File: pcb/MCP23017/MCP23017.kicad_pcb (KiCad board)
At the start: 2 copper layers, 15 parts, among them U1 MCP23017, U2 Header2

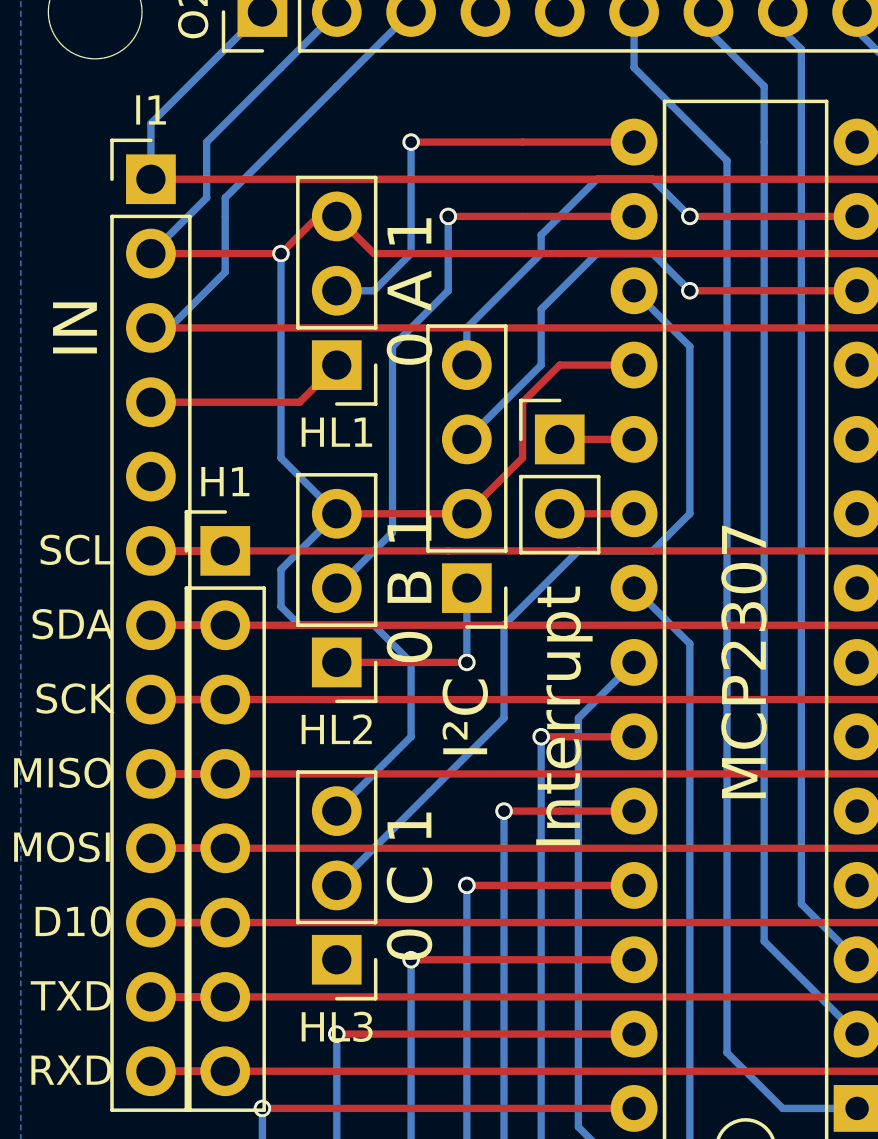
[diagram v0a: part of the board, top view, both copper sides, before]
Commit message: Added a new "power" and LEDs module (split into two half size modules)
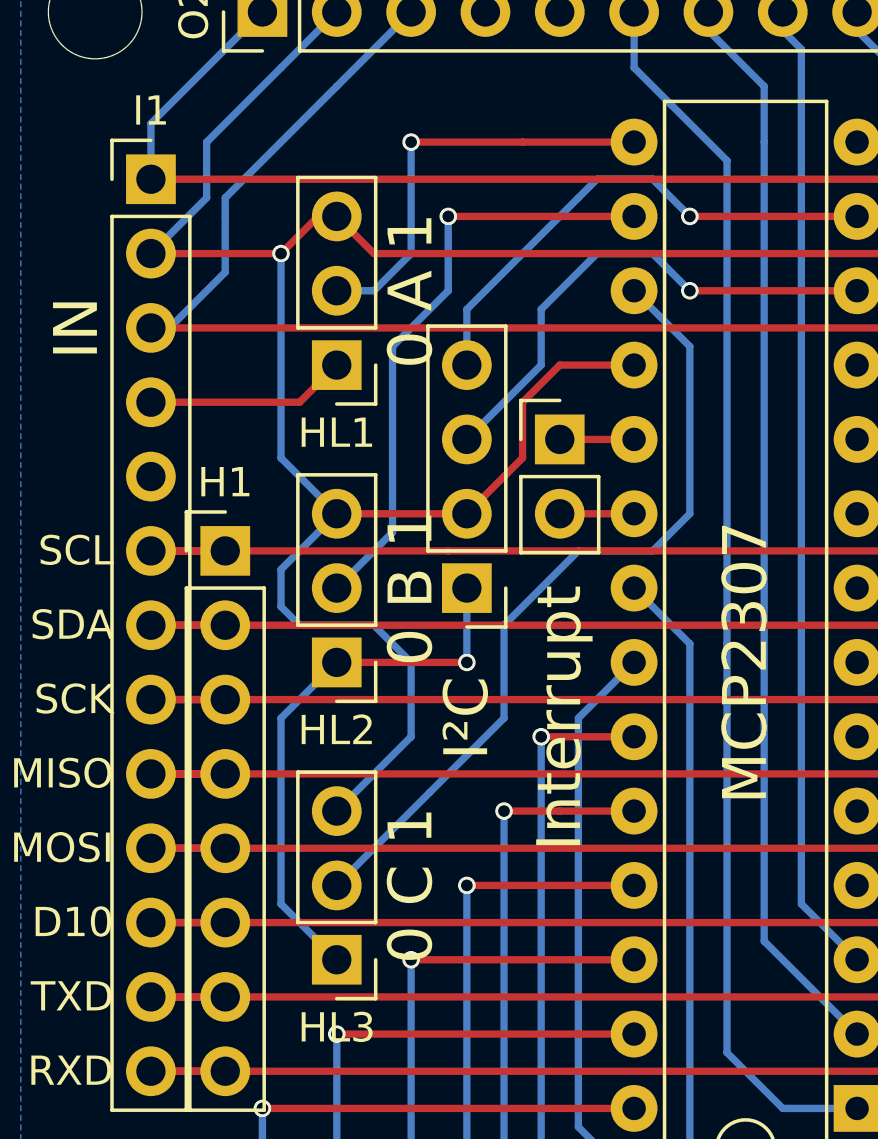
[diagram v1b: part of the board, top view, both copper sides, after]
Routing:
- net Earth: track 14.5 -> 26.2 mm
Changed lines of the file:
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@@
   (general
     (links 62)
-    (no_connects 0)
+    (no_connects 1)
     (area 124.46 82.55 173.990001 132.16)
     (thickness 1.6)
     (drawings 19)
-    (tracks 208)
+    (tracks 211)
     (zones 0)
     (modules 15)
@@
   (segment (start 160.655 97.155) (end 160.655 125.095) (width 0.25) (layer B.Cu) (net 3))
   (via (at 160.655 97.155) (size 0.6) (drill 0.4) (layers F.Cu B.Cu) (net 3))
+  (segment (start 136.525 108.585) (end 134.62 110.49) (width 0.25) (layer B.Cu) (net 4) (status 400000))
+  (segment (start 134.62 116.84) (end 136.525 118.745) (width 0.25) (layer B.Cu) (net 4) (status 800000))
+  (segment (start 134.62 110.49) (end 134.62 116.84) (width 0.25) (layer B.Cu) (net 4))
   (segment (start 136.525 108.585) (end 140.97 108.585) (width 0.25) (layer F.Cu) (net 4))
   (segment (start 140.97 108.585) (end 140.97 106.045) (width 0.25) (layer B.Cu) (net 4))
@@
   (segment (start 130.175 104.775) (end 140.335 104.775) (width 0.25) (layer F.Cu) (net 5))
   (segment (start 140.335 104.775) (end 168.275 104.775) (width 0.25) (layer F.Cu) (net 5))
+  (segment (start 140.97 97.155) (end 140.97 96.52) (width 0.25) (layer B.Cu) (net 6))
+  (segment (start 140.97 96.52) (end 144.78 92.71) (width 0.25) (layer B.Cu) (net 6))
   (segment (start 130.175 107.315) (end 132.715 107.315) (width 0.25) (layer F.Cu) (net 6) (status C00000))
-  (segment (start 140.97 97.155) (end 143.51 94.615) (width 0.25) (layer B.Cu) (net 6))
-  (segment (start 143.51 94.615) (end 143.51 93.98) (width 0.25) (layer B.Cu) (net 6))
   (segment (start 147.32 92.075) (end 148.59 93.345) (width 0.25) (layer B.Cu) (net 6))
   (segment (start 145.415 92.075) (end 147.32 92.075) (width 0.25) (layer B.Cu) (net 6))
-  (segment (start 143.51 93.98) (end 145.415 92.075) (width 0.25) (layer B.Cu) (net 6))
+  (segment (start 144.78 92.71) (end 145.415 92.075) (width 0.25) (layer B.Cu) (net 6))
   (segment (start 140.97 98.425) (end 140.97 97.155) (width 0.25) (layer B.Cu) (net 6))
   (segment (start 148.59 93.345) (end 154.305 93.345) (width 0.25) (layer F.Cu) (net 6))

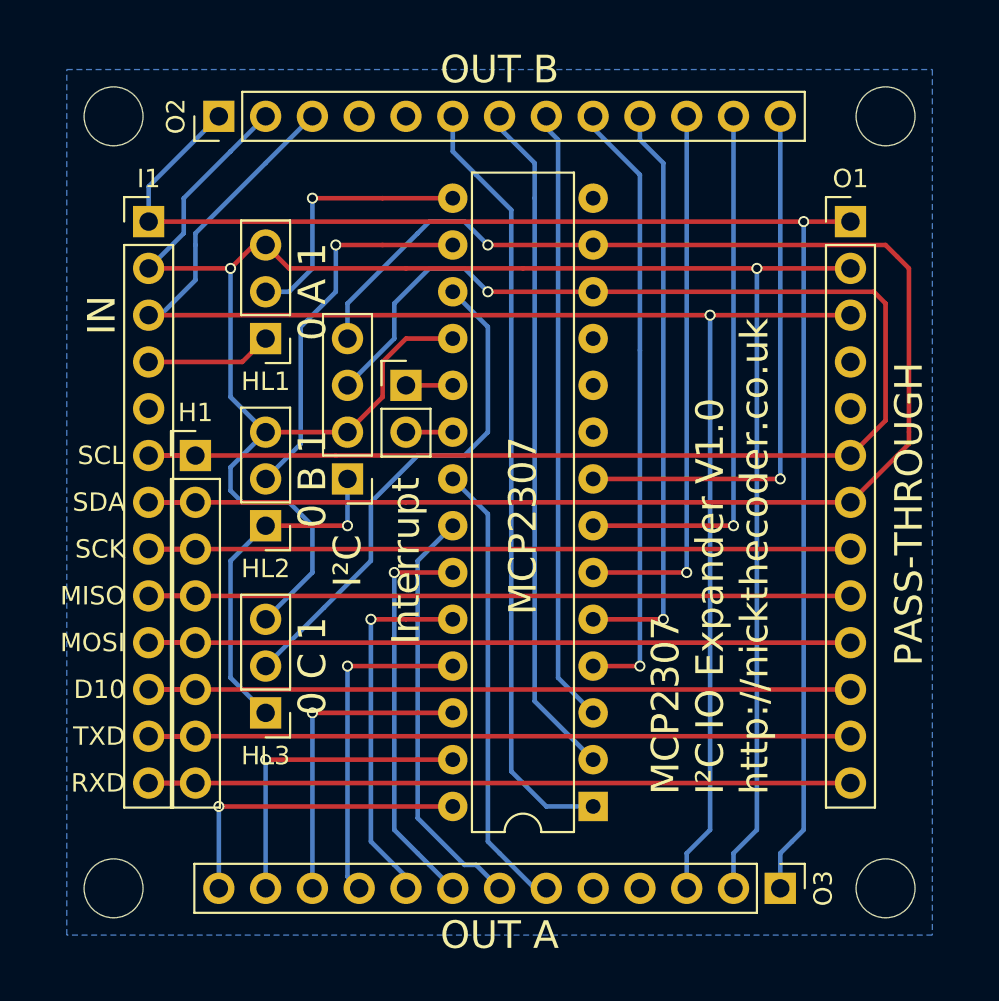
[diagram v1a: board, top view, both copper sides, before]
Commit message: Reworked the MCP23017 I2C IO Expander module.
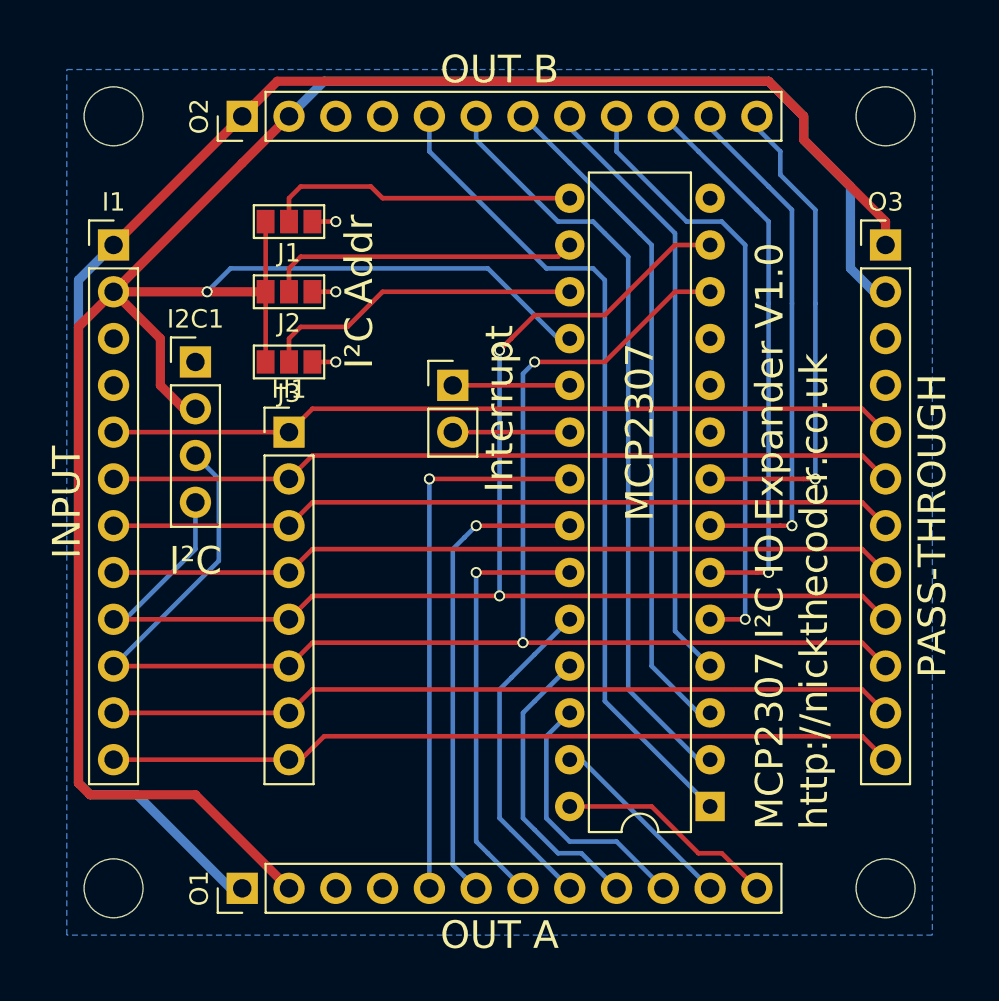
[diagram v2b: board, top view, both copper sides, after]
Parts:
- removed HL1, HL2, HL3: High-Low, Pin_Headers:Pin_Header_Straight_1x03_Pitch2.54mm
- added J1: GS3, Connectors:GS3, F.Cu at (137.8, 92.1)
- added J2: GS3, Connectors:GS3, F.Cu at (137.8, 95.9)
- added J3: GS3, Connectors:GS3, F.Cu at (137.8, 99.7)
- I1: value ePlayInput -> SerialInput; footprint Pin_Headers:Pin_Header_Straight_1x13_Pitch2.54mm -> Socket_Strips:Socket_Strip_Straight_1x12_Pitch2.54mm
- O1, O2: value ePlayOutput -> Output; footprint Socket_Strips:Socket_Strip_Straight_1x13_Pitch2.54mm -> Socket_Strips:Socket_Strip_Straight_1x12_Pitch2.54mm
- O3: value ePlayOutput -> SerialOutput; footprint Socket_Strips:Socket_Strip_Straight_1x13_Pitch2.54mm -> Socket_Strips:Socket_Strip_Straight_1x12_Pitch2.54mm
- moved O1 49.0 mm to (135.3, 128.3), turned to 90 degrees
- moved O3 35.4 mm to (170.2, 93.3), turned to 0 degrees
- moved I2C1 10.4 mm to (132.7, 99.7), turned to 0 degrees
- moved U1 6.35 mm to (160.7, 123.8)
- moved H1 5.24 mm to (137.8, 103.5)
- moved U2 2.54 mm to (146.7, 101.0)
- moved I1 2.29 mm to (128.3, 93.3)
- moved O2 1.27 mm to (135.3, 86.4)
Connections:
- I1 pad 10: /L4 -> /L5
- I1 pad 11: /L5 -> /L6
- I1 pad 12: /L6 -> /L7
- I1 pad 3: /3V3 -> Earth
- I1 pad 4: Earth -> (no net)
- I1 pad 5: (no net) -> /L0
- I1 pad 6: /L0 -> /L1
- I1 pad 7: /L1 -> /L2
- I1 pad 8: /L2 -> /L3
- I1 pad 9: /L3 -> /L4
- I2C1 pad 3: /L0 -> /L5
- I2C1 pad 4: /L1 -> /L4
- O1 pad 10: /L4 -> Net-(O1-Pad10)
- O1 pad 11: /L5 -> Net-(O1-Pad11)
- O1 pad 12: /L6 -> Net-(O1-Pad12)
- O1 pad 3: /3V3 -> Earth
- O1 pad 4: Earth -> (no net)
- O1 pad 5: (no net) -> Net-(O1-Pad5)
- O1 pad 6: /L0 -> Net-(O1-Pad6)
- O1 pad 7: /L1 -> Net-(O1-Pad7)
- O1 pad 8: /L2 -> Net-(O1-Pad8)
- O1 pad 9: /L3 -> Net-(O1-Pad9)
- O2 pad 3: /3V3 -> Earth
- O2 pad 4: Earth -> (no net)
- O2 pad 5: (no net) -> Net-(O2-Pad5)
- O3 pad 10: Net-(O3-Pad10) -> /L5
- O3 pad 11: Net-(O3-Pad11) -> /L6
- O3 pad 12: Net-(O3-Pad12) -> /L7
- O3 pad 3: /3V3 -> Earth
- O3 pad 4: Earth -> (no net)
- O3 pad 5: (no net) -> /L0
- O3 pad 6: Net-(O3-Pad6) -> /L1
- O3 pad 7: Net-(O3-Pad7) -> /L2
- O3 pad 8: Net-(O3-Pad8) -> /L3
- O3 pad 9: Net-(O3-Pad9) -> /L4
- U1 pad 1: Net-(O2-Pad6) -> Net-(O2-Pad5)
- U1 pad 12: /L0 -> /L5
- U1 pad 13: /L1 -> /L4
- U1 pad 2: Net-(O2-Pad7) -> Net-(O2-Pad6)
- U1 pad 21: Net-(O3-Pad6) -> Net-(O1-Pad5)
- U1 pad 22: Net-(O3-Pad7) -> Net-(O1-Pad6)
- U1 pad 23: Net-(O3-Pad8) -> Net-(O1-Pad7)
- U1 pad 24: Net-(O3-Pad9) -> Net-(O1-Pad8)
- U1 pad 25: Net-(O3-Pad10) -> Net-(O1-Pad9)
- U1 pad 26: Net-(O3-Pad11) -> Net-(O1-Pad10)
- U1 pad 27: Net-(O3-Pad12) -> Net-(O1-Pad11)
- U1 pad 28: Net-(O3-Pad13) -> Net-(O1-Pad12)
- U1 pad 3: Net-(O2-Pad8) -> Net-(O2-Pad7)
- U1 pad 4: Net-(O2-Pad9) -> Net-(O2-Pad8)
- U1 pad 5: Net-(O2-Pad10) -> Net-(O2-Pad9)
- U1 pad 6: Net-(O2-Pad11) -> Net-(O2-Pad10)
- U1 pad 7: Net-(O2-Pad12) -> Net-(O2-Pad11)
- U1 pad 8: Net-(O2-Pad13) -> Net-(O2-Pad12)
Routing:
- net /3V3: track 84.6 -> 0.00 mm, vias 1 -> 0
- net /L1: track 89.9 -> 43.6 mm, vias 1 -> 0
- net Net-(O2-Pad5): track 0.00 -> 45.3 mm
- net /L5: track 40.6 -> 83.9 mm, vias 0 -> 2
- net /L0: track 84.7 -> 43.0 mm, vias 1 -> 0
- net /L4: track 40.6 -> 78.7 mm, vias 0 -> 2
- net Net-(O1-Pad5): track 0.00 -> 29.8 mm, vias 0 -> 1
- net Net-(O2-Pad13): track 29.8 -> 0.00 mm, vias 1 -> 0
- net Net-(O1-Pad6): track 0.00 -> 25.8 mm, vias 0 -> 1
- net Net-(O3-Pad6): track 24.7 -> 0.00 mm
- net Net-(O1-Pad7): track 0.00 -> 23.3 mm, vias 0 -> 1
- net Net-(O3-Pad7): track 22.7 -> 0.00 mm
- net Earth: track 26.2 -> 3.81 mm, vias 1 -> 3
- net Net-(O3-Pad8): track 21.6 -> 0.00 mm, vias 1 -> 0
- net Net-(O3-Pad9): track 19.8 -> 0.00 mm, vias 1 -> 0
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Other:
- board text added: "INPUT"
- board text added: "I²C Addr"
- board text removed: "0 A 1"
- board text removed: "0 B 1"
- board text removed: "0 C 1"
- board text removed: "D10"
- board text removed: "IN"
- board text removed: "MISO"
- board text removed: "MOSI"
- board text removed: "RXD"
- board text removed: "SCK"
- board text removed: "SCL"
- board text removed: "SDA"
- board text removed: "TXD"

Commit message: Added a multiplexer module (which works in master and slave mode, for up to 40:1 with 5 boards)
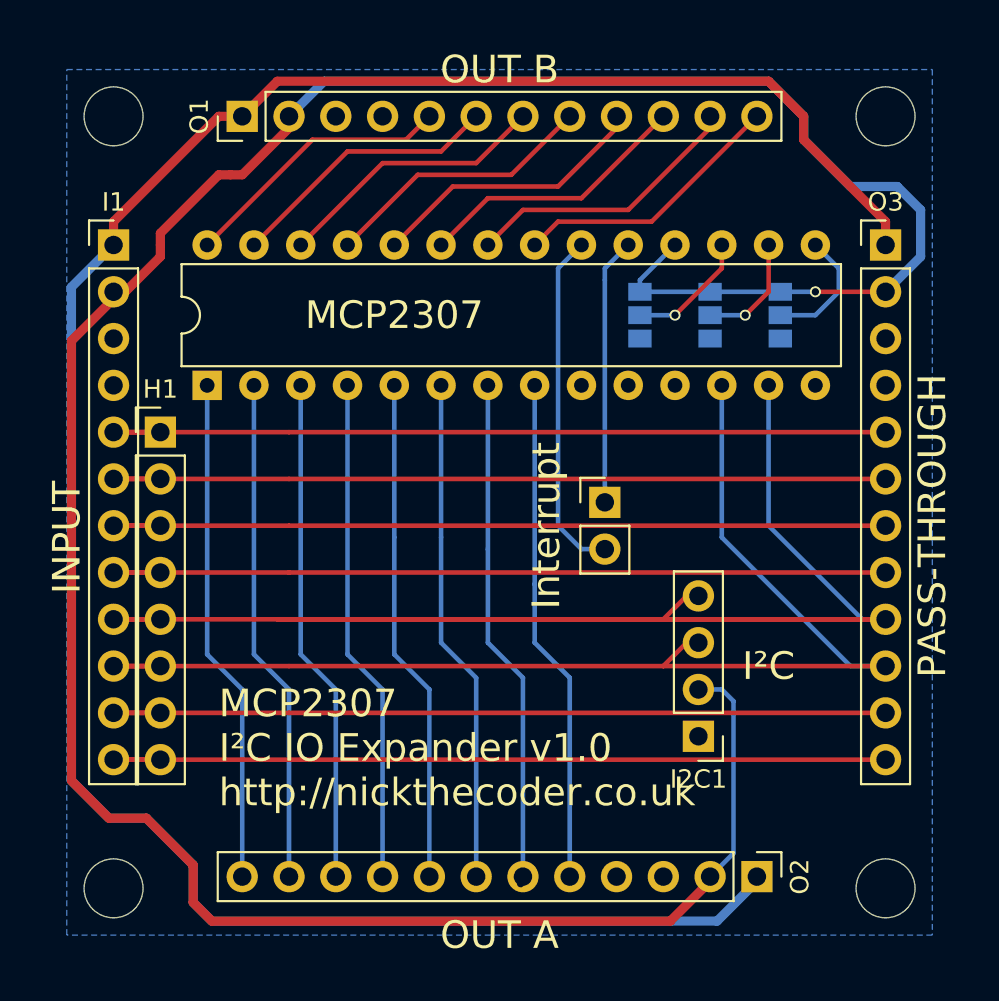
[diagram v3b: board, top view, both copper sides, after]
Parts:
- J1, J2, J3: moved to B.Cu
- moved O2 49.8 mm to (163.2, 127.6), turned to 270 degrees
- moved O1 41.9 mm to (135.3, 86.4)
- moved U1 35.6 mm to (133.3, 101.0), turned to 90 degrees
- moved I2C1 34.0 mm to (160.0, 120.0), turned to 180 degrees
- moved J1 27.1 mm to (164.5, 97.2), turned to 180 degrees
- moved J2 22.9 mm to (160.7, 97.2), turned to 180 degrees
- moved J3 19.2 mm to (156.8, 97.2), turned to 180 degrees
- moved U2 10.4 mm to (154.9, 107.3)
- moved H1 6.98 mm to (130.8, 103.5)
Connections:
- U1 pad 1: Net-(O2-Pad5) -> Net-(O2-Pad12)
- U1 pad 2: Net-(O2-Pad6) -> Net-(O2-Pad11)
- U1 pad 21: Net-(O1-Pad5) -> Net-(O1-Pad12)
- U1 pad 22: Net-(O1-Pad6) -> Net-(O1-Pad11)
- U1 pad 23: Net-(O1-Pad7) -> Net-(O1-Pad10)
- U1 pad 24: Net-(O1-Pad8) -> Net-(O1-Pad9)
- U1 pad 25: Net-(O1-Pad9) -> Net-(O1-Pad8)
- U1 pad 26: Net-(O1-Pad10) -> Net-(O1-Pad7)
- U1 pad 27: Net-(O1-Pad11) -> Net-(O1-Pad6)
- U1 pad 28: Net-(O1-Pad12) -> Net-(O1-Pad5)
- U1 pad 3: Net-(O2-Pad7) -> Net-(O2-Pad10)
- U1 pad 4: Net-(O2-Pad8) -> Net-(O2-Pad9)
- U1 pad 5: Net-(O2-Pad9) -> Net-(O2-Pad8)
- U1 pad 6: Net-(O2-Pad10) -> Net-(O2-Pad7)
- U1 pad 7: Net-(O2-Pad11) -> Net-(O2-Pad6)
- U1 pad 8: Net-(O2-Pad12) -> Net-(O2-Pad5)
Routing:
- net /VIN: track 92.0 -> 123.8 mm
- net /L4: track 78.7 -> 96.6 mm, vias 2 -> 0
- net Net-(O2-Pad5): track 45.3 -> 27.6 mm
- net /L5: track 83.9 -> 66.9 mm, vias 2 -> 0
- net Net-(O1-Pad5): track 29.8 -> 15.0 mm, vias 1 -> 0
- net Net-(O2-Pad6): track 41.7 -> 27.5 mm, vias 0 -> 1
- net Net-(U1-Pad20): track 6.35 -> 18.8 mm
- net /VCC: track 142.2 -> 154.6 mm
- net Net-(O1-Pad6): track 25.8 -> 15.0 mm, vias 1 -> 0
- net Net-(J2-Pad2): track 17.0 -> 6.24 mm, vias 0 -> 1
- net Net-(J3-Pad2): track 17.6 -> 6.77 mm, vias 0 -> 1
- net Net-(J1-Pad2): track 17.0 -> 6.77 mm
- net Net-(O2-Pad7): track 37.0 -> 27.5 mm
- net Net-(U1-Pad19): track 6.35 -> 15.1 mm
- net Net-(O1-Pad7): track 23.3 -> 15.0 mm, vias 1 -> 0
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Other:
- board text added: "0"
- board text added: "1"
- board text added: "MCP2307 I²C IO Expander v1.0 http://nickthecoder.co.uk"
- board text removed: "MCP2307 I²C IO Expander V1.0 http://nickthecoder.co.uk"
